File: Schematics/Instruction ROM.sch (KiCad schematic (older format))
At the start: 4 parts

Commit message: annotate
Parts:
- gave numbers to parts that had none: 4
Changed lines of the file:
@@
 $EndDescr
 $Comp
-L Memory_EEPROM:GLS29EE010 U?
+L Memory_EEPROM:GLS29EE010 U26
 U 1 1 5D23BFD4
 P 4500 2000
-F 0 "U?" H 4800 2200 50  0000 C CNN
+F 0 "U26" H 4800 2200 50  0000 C CNN
 F 1 "GLS29EE010" H 4800 2100 50  0000 C CNN
 F 2 "" H 4500 2000 50  0001 C CNN
@@
 $EndComp
 $Comp
-L power:VCC #PWR?
+L power:VCC #PWR0158
 U 1 1 5D241E73
 P 4500 1000
-F 0 "#PWR?" H 4500 850 50  0001 C CNN
+F 0 "#PWR0158" H 4500 850 50  0001 C CNN
 F 1 "VCC" H 4517 1173 50  0000 C CNN
 F 2 "" H 4500 1000 50  0001 C CNN
@@
 	4500 1500 4500 1900
 $Comp
-L power:GND #PWR?
+L power:GND #PWR0159
 U 1 1 5D2423FD
 P 4500 5000
-F 0 "#PWR?" H 4500 4750 50  0001 C CNN
+F 0 "#PWR0159" H 4500 4750 50  0001 C CNN
 F 1 "GND" H 4505 4827 50  0000 C CNN
 F 2 "" H 4500 5000 50  0001 C CNN
@@
 	7550 1700 8450 1700
 $Comp
-L Device:C C?
+L Device:C C23
 U 1 1 5DCD89FF
 P 1150 7300
-F 0 "C?" H 1265 7346 50  0000 L CNN
+F 0 "C23" H 1265 7346 50  0000 L CNN
 F 1 "100nF" H 1265 7255 50  0000 L CNN
 F 2 "" H 1188 7150 50  0001 C CNN
@@
 $EndComp
 $Comp
-L Device:C C?
+L Device:C C24
 U 1 1 5DCD8A05
 P 1650 7300
-F 0 "C?" H 1765 7346 50  0000 L CNN
+F 0 "C24" H 1765 7346 50  0000 L CNN
 F 1 "100nF" H 1765 7255 50  0000 L CNN
 F 2 "" H 1688 7150 50  0001 C CNN
@@
 $EndComp
 $Comp
-L power:GND #PWR?
+L power:GND #PWR0160
 U 1 1 5DCD8A1D
 P 1150 7450
-F 0 "#PWR?" H 1150 7200 50  0001 C CNN
+F 0 "#PWR0160" H 1150 7200 50  0001 C CNN
 F 1 "GND" H 1155 7277 50  0000 C CNN
 F 2 "" H 1150 7450 50  0001 C CNN
@@
 $EndComp
 $Comp
-L power:VCC #PWR?
+L power:VCC #PWR0161
 U 1 1 5DCD8A23
 P 1150 7150
-F 0 "#PWR?" H 1150 7000 50  0001 C CNN
+F 0 "#PWR0161" H 1150 7000 50  0001 C CNN
 F 1 "VCC" H 1167 7323 50  0000 C CNN
 F 2 "" H 1150 7150 50  0001 C CNN
@@
 Connection ~ 1150 7450
 $Comp
-L Memory_EEPROM:GLS29EE010 U?
+L Memory_EEPROM:GLS29EE010 U27
 U 1 1 5D23ED7B
 P 6550 2000
-F 0 "U?" H 6250 2200 50  0000 C CNN
+F 0 "U27" H 6250 2200 50  0000 C CNN
 F 1 "GLS29EE010" H 6250 2100 50  0000 C CNN
 F 2 "" H 6550 2000 50  0001 C CNN

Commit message: Add footprints to all decoupling caps
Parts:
- C23, C24: footprint (none) -> Capacitor_THT:C_Disc_D4.3mm_W1.9mm_P5.00mm
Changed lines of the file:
@@
 F 0 "C23" H 1265 7346 50  0000 L CNN
 F 1 "100nF" H 1265 7255 50  0000 L CNN
-F 2 "" H 1188 7150 50  0001 C CNN
+F 2 "Capacitor_THT:C_Disc_D4.3mm_W1.9mm_P5.00mm" H 1188 7150 50  0001 C CNN
 F 3 "~" H 1150 7300 50  0001 C CNN
 	1    1150 7300
@@
 F 0 "C24" H 1765 7346 50  0000 L CNN
 F 1 "100nF" H 1765 7255 50  0000 L CNN
-F 2 "" H 1688 7150 50  0001 C CNN
+F 2 "Capacitor_THT:C_Disc_D4.3mm_W1.9mm_P5.00mm" H 1688 7150 50  0001 C CNN
 F 3 "~" H 1650 7300 50  0001 C CNN
 	1    1650 7300

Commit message: Assign a bunch more footprints. All are assigned now.
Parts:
- U26, U27: footprint (none) -> Package_DIP:DIP-32_W15.24mm_Socket
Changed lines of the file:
@@
 F 0 "U26" H 4800 2200 50  0000 C CNN
 F 1 "GLS29EE010" H 4800 2100 50  0000 C CNN
-F 2 "" H 4500 2000 50  0001 C CNN
+F 2 "Package_DIP:DIP-32_W15.24mm_Socket" H 4500 2000 50  0001 C CNN
 F 3 "" H 4500 2000 50  0001 C CNN
 	1    4500 2000
@@
 F 0 "U27" H 6250 2200 50  0000 C CNN
 F 1 "GLS29EE010" H 6250 2100 50  0000 C CNN
-F 2 "" H 6550 2000 50  0001 C CNN
+F 2 "Package_DIP:DIP-32_W15.24mm_Socket" H 6550 2000 50  0001 C CNN
 F 3 "" H 6550 2000 50  0001 C CNN
 	1    6550 2000

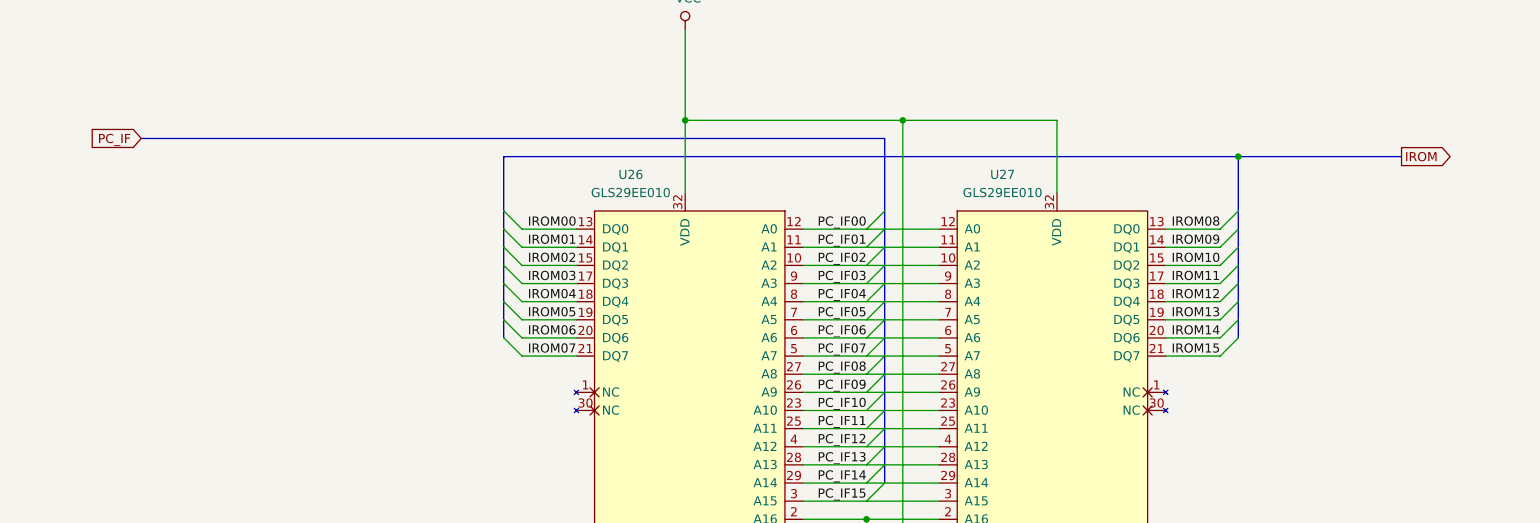
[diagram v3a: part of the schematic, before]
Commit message: My buses were not named according the rules in the Eeschema manual.
Buses which connect to global labels must be named specially.
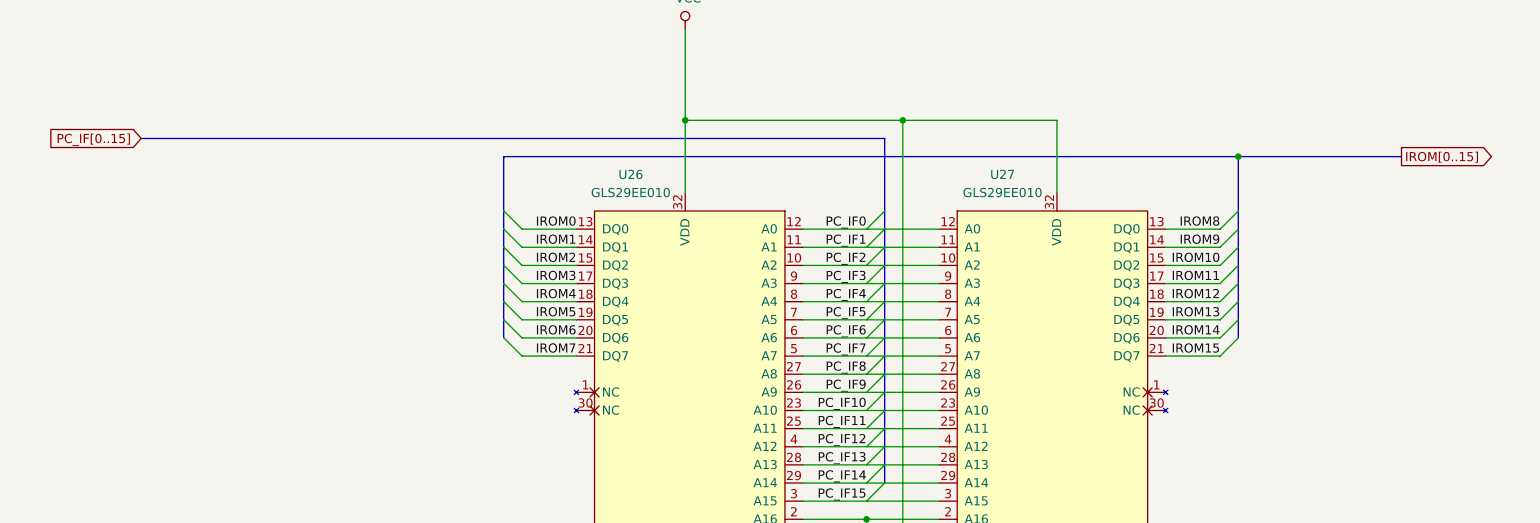
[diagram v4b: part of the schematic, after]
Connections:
- net IROM00 renamed IROM0
- net IROM01 renamed IROM1
- net IROM02 renamed IROM2
- net IROM03 renamed IROM3
- net IROM04 renamed IROM4
- net IROM05 renamed IROM5
- net IROM06 renamed IROM6
- net IROM07 renamed IROM7
- net IROM08 renamed IROM8
- net IROM09 renamed IROM9
- net PC_IF00 renamed PC_IF0
- net PC_IF01 renamed PC_IF1
- net PC_IF02 renamed PC_IF2
- net PC_IF03 renamed PC_IF3
- net PC_IF04 renamed PC_IF4
- net PC_IF05 renamed PC_IF5
- net PC_IF06 renamed PC_IF6
- net PC_IF07 renamed PC_IF7
- net PC_IF08 renamed PC_IF8
- net PC_IF09 renamed PC_IF9
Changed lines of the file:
@@
 	5500 3600 5600 3500
 Text Label 5500 2100 2    50   ~ 0
-PC_IF00
+PC_IF0
 Text Label 5500 2200 2    50   ~ 0
-PC_IF01
+PC_IF1
 Text Label 5500 2300 2    50   ~ 0
-PC_IF02
+PC_IF2
 Text Label 5500 2400 2    50   ~ 0
-PC_IF03
+PC_IF3
 Text Label 5500 2500 2    50   ~ 0
-PC_IF04
+PC_IF4
 Text Label 5500 2600 2    50   ~ 0
-PC_IF05
+PC_IF5
 Text Label 5500 2700 2    50   ~ 0
-PC_IF06
+PC_IF6
 Text Label 5500 2800 2    50   ~ 0
-PC_IF07
+PC_IF7
 Text Label 5500 2900 2    50   ~ 0
-PC_IF08
+PC_IF8
 Text Label 5500 3000 2    50   ~ 0
-PC_IF09
+PC_IF9
 Text Label 5500 3100 2    50   ~ 0
 PC_IF10
@@
 	7450 2800 7150 2800
 Text Label 7450 2100 2    50   ~ 0
-IROM08
+IROM8
 Text Label 7450 2200 2    50   ~ 0
-IROM09
+IROM9
 Text Label 3900 2500 2    50   ~ 0
-IROM04
+IROM4
 Text Label 3900 2600 2    50   ~ 0
-IROM05
+IROM5
 Text Label 3900 2700 2    50   ~ 0
-IROM06
+IROM6
 Text Label 3900 2800 2    50   ~ 0
-IROM07
+IROM7
 Text Label 7450 2300 2    50   ~ 0
 IROM10
@@
 IROM15
 Text GLabel 8450 1700 2    50   Output ~ 0
-IROM
+IROM[0..15]
 Text GLabel 1500 1600 0    50   Input ~ 0
-PC_IF
+PC_IF[0..15]
 Wire Wire Line
 	6550 1500 5700 1500
 Text Label 3900 2400 2    50   ~ 0
-IROM03
+IROM3
 Text Label 3900 2300 2    50   ~ 0
-IROM02
+IROM2
 Text Label 3900 2200 2    50   ~ 0
-IROM01
+IROM1
 Text Label 3900 2100 2    50   ~ 0
-IROM00
+IROM0
 Wire Wire Line
 	3600 2100 3900 2100

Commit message: Add unused IC units to Output Display to ensure no ICs are shared with other modules.
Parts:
- renumbered U26 to U25, U27 to U26
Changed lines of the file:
@@
 $EndDescr
 $Comp
-L Memory_EEPROM:GLS29EE010 U26
+L Memory_EEPROM:GLS29EE010 U25
 U 1 1 5D23BFD4
 P 4500 2000
-F 0 "U26" H 4800 2200 50  0000 C CNN
+F 0 "U25" H 4800 2200 50  0000 C CNN
 F 1 "GLS29EE010" H 4800 2100 50  0000 C CNN
 F 2 "Package_DIP:DIP-32_W15.24mm_Socket" H 4500 2000 50  0001 C CNN
@@
 $EndComp
 $Comp
-L power:VCC #PWR0158
+L power:VCC #PWR060
 U 1 1 5D241E73
 P 4500 1000
-F 0 "#PWR0158" H 4500 850 50  0001 C CNN
+F 0 "#PWR060" H 4500 850 50  0001 C CNN
 F 1 "VCC" H 4517 1173 50  0000 C CNN
 F 2 "" H 4500 1000 50  0001 C CNN
@@
 	4500 1500 4500 1900
 $Comp
-L power:GND #PWR0159
+L power:GND #PWR061
 U 1 1 5D2423FD
 P 4500 5000
-F 0 "#PWR0159" H 4500 4750 50  0001 C CNN
+F 0 "#PWR061" H 4500 4750 50  0001 C CNN
 F 1 "GND" H 4505 4827 50  0000 C CNN
 F 2 "" H 4500 5000 50  0001 C CNN
@@
 $EndComp
 $Comp
-L power:GND #PWR0160
+L power:GND #PWR059
 U 1 1 5DCD8A1D
 P 1150 7450
-F 0 "#PWR0160" H 1150 7200 50  0001 C CNN
+F 0 "#PWR059" H 1150 7200 50  0001 C CNN
 F 1 "GND" H 1155 7277 50  0000 C CNN
 F 2 "" H 1150 7450 50  0001 C CNN
@@
 $EndComp
 $Comp
-L power:VCC #PWR0161
+L power:VCC #PWR058
 U 1 1 5DCD8A23
 P 1150 7150
-F 0 "#PWR0161" H 1150 7000 50  0001 C CNN
+F 0 "#PWR058" H 1150 7000 50  0001 C CNN
 F 1 "VCC" H 1167 7323 50  0000 C CNN
 F 2 "" H 1150 7150 50  0001 C CNN
@@
 Connection ~ 1150 7450
 $Comp
-L Memory_EEPROM:GLS29EE010 U27
+L Memory_EEPROM:GLS29EE010 U26
 U 1 1 5D23ED7B
 P 6550 2000
-F 0 "U27" H 6250 2200 50  0000 C CNN
+F 0 "U26" H 6250 2200 50  0000 C CNN
 F 1 "GLS29EE010" H 6250 2100 50  0000 C CNN
 F 2 "Package_DIP:DIP-32_W15.24mm_Socket" H 6550 2000 50  0001 C CNN

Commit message: Add unused IC units to Data RAM to ensure no ICs are shared with other modules.
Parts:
- renumbered U25 to U24, U26 to U25
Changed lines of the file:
@@
 $EndDescr
 $Comp
-L Memory_EEPROM:GLS29EE010 U25
+L Memory_EEPROM:GLS29EE010 U24
 U 1 1 5D23BFD4
 P 4500 2000
-F 0 "U25" H 4800 2200 50  0000 C CNN
+F 0 "U24" H 4800 2200 50  0000 C CNN
 F 1 "GLS29EE010" H 4800 2100 50  0000 C CNN
 F 2 "Package_DIP:DIP-32_W15.24mm_Socket" H 4500 2000 50  0001 C CNN
@@
 Connection ~ 1150 7450
 $Comp
-L Memory_EEPROM:GLS29EE010 U26
+L Memory_EEPROM:GLS29EE010 U25
 U 1 1 5D23ED7B
 P 6550 2000
-F 0 "U26" H 6250 2200 50  0000 C CNN
+F 0 "U25" H 6250 2200 50  0000 C CNN
 F 1 "GLS29EE010" H 6250 2100 50  0000 C CNN
 F 2 "Package_DIP:DIP-32_W15.24mm_Socket" H 6550 2000 50  0001 C CNN

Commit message: Pack parts neatly into a smaller board size.
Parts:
- renumbered C23 to C24, C24 to C25
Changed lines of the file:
@@
 $EndComp
 $Comp
-L power:VCC #PWR060
+L power:VCC #PWR062
 U 1 1 5D241E73
 P 4500 1000
-F 0 "#PWR060" H 4500 850 50  0001 C CNN
+F 0 "#PWR062" H 4500 850 50  0001 C CNN
 F 1 "VCC" H 4517 1173 50  0000 C CNN
 F 2 "" H 4500 1000 50  0001 C CNN
@@
 	4500 1500 4500 1900
 $Comp
-L power:GND #PWR061
+L power:GND #PWR063
 U 1 1 5D2423FD
 P 4500 5000
-F 0 "#PWR061" H 4500 4750 50  0001 C CNN
+F 0 "#PWR063" H 4500 4750 50  0001 C CNN
 F 1 "GND" H 4505 4827 50  0000 C CNN
 F 2 "" H 4500 5000 50  0001 C CNN
@@
 	7550 1700 8450 1700
 $Comp
-L Device:C C23
+L Device:C C24
 U 1 1 5DCD89FF
 P 1150 7300
-F 0 "C23" H 1265 7346 50  0000 L CNN
+F 0 "C24" H 1265 7346 50  0000 L CNN
 F 1 "100nF" H 1265 7255 50  0000 L CNN
 F 2 "Capacitor_THT:C_Disc_D4.3mm_W1.9mm_P5.00mm" H 1188 7150 50  0001 C CNN
@@
 $EndComp
 $Comp
-L Device:C C24
+L Device:C C25
 U 1 1 5DCD8A05
 P 1650 7300
-F 0 "C24" H 1765 7346 50  0000 L CNN
+F 0 "C25" H 1765 7346 50  0000 L CNN
 F 1 "100nF" H 1765 7255 50  0000 L CNN
 F 2 "Capacitor_THT:C_Disc_D4.3mm_W1.9mm_P5.00mm" H 1688 7150 50  0001 C CNN
@@
 $EndComp
 $Comp
-L power:GND #PWR059
+L power:GND #PWR061
 U 1 1 5DCD8A1D
 P 1150 7450
-F 0 "#PWR059" H 1150 7200 50  0001 C CNN
+F 0 "#PWR061" H 1150 7200 50  0001 C CNN
 F 1 "GND" H 1155 7277 50  0000 C CNN
 F 2 "" H 1150 7450 50  0001 C CNN
@@
 $EndComp
 $Comp
-L power:VCC #PWR058
+L power:VCC #PWR060
 U 1 1 5DCD8A23
 P 1150 7150
-F 0 "#PWR058" H 1150 7000 50  0001 C CNN
+F 0 "#PWR060" H 1150 7000 50  0001 C CNN
 F 1 "VCC" H 1167 7323 50  0000 C CNN
 F 2 "" H 1150 7150 50  0001 C CNN
